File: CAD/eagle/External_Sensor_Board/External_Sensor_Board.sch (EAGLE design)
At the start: 14 parts, among them J1 SFW15R_FFC, J2 J30J-25, U1 MAX31725MTA+, U2 HSCMNNN1.6BAAA3, U3 P82B715

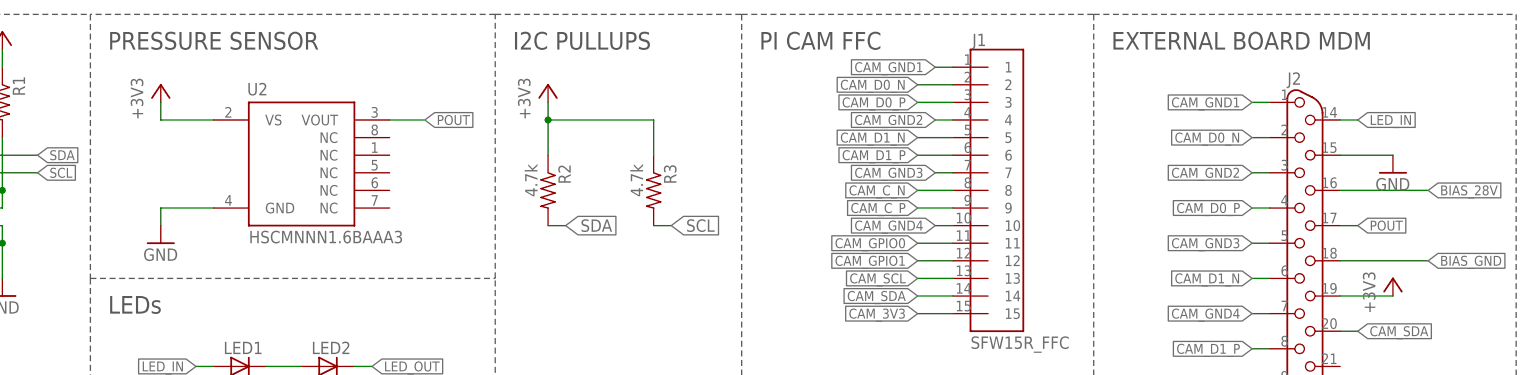
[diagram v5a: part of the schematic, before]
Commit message: Began work on pressure sensor library. Realized I specced an inadequate sensor. Specced a better sensor (in the same family). Changed external sensor board to compensate.
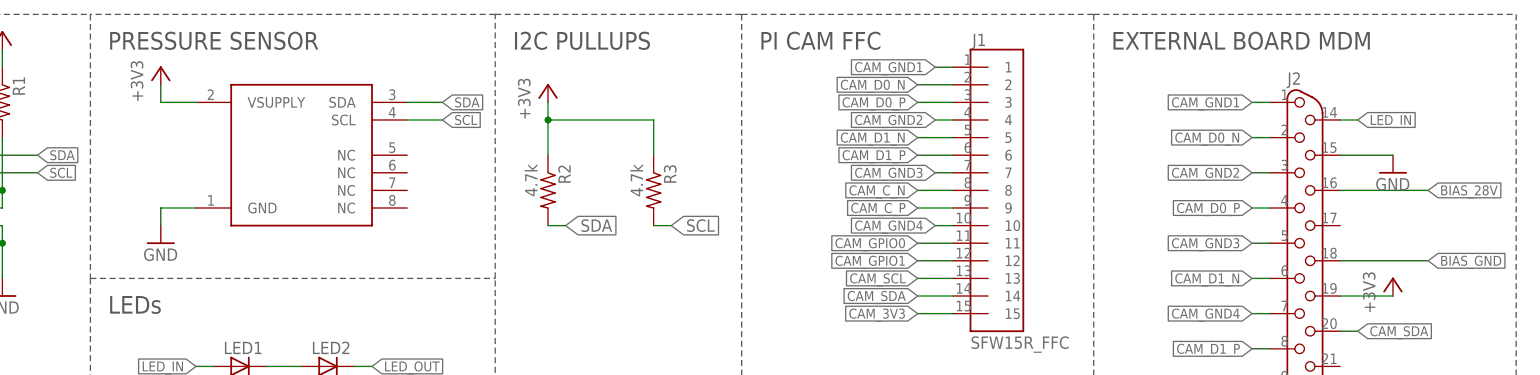
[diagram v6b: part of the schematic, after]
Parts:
- U2: value HSCMNNN1.6BAAA3 -> SSCMNNN015PA2A3; device NR_IC:HSCMNNN1.6BAAA3 -> NR_IC:SSCMNNN015PA2A3
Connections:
- removed net POUT: J2.17, U2.VOUT
- net +3V3: now also U2.VSUPPLY; no longer U2.VS
- net SCL: now also U2.SCL
- net SDA: now also U2.SDA
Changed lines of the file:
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@@
 <part name="R1" library="resistor" deviceset="R-US_" device="R0603" value="4.7k"/>
 <part name="GND2" library="supply1" deviceset="GND" device=""/>
-<part name="U2" library="NR_IC" deviceset="HSCMNNN1.6BAAA3" device=""/>
 <part name="+3V3" library="supply1" deviceset="+3V3" device=""/>
 <part name="GND3" library="supply1" deviceset="GND" device=""/>
@@
 <part name="GND7" library="supply1" deviceset="GND" device=""/>
 <part name="JP1" library="pinhead" deviceset="PINHD-1X2" device=""/>
+<part name="U2" library="NR_IC" deviceset="SSCMNNN015PA2A3" device=""/>
 </parts>
 <sheets>
@@
 <instance part="R1" gate="G$1" x="55.88" y="195.58" rot="R270"/>
 <instance part="GND2" gate="1" x="55.88" y="167.64"/>
-<instance part="U2" gate="G$1" x="99.06" y="187.96"/>
-<instance part="+3V3" gate="G$1" x="78.74" y="198.12"/>
+<instance part="+3V3" gate="G$1" x="78.74" y="200.66"/>
 <instance part="GND3" gate="1" x="78.74" y="175.26"/>
 <instance part="+3V4" gate="G$1" x="134.62" y="198.12"/>
@@
 <instance part="GND7" gate="1" x="256.54" y="185.42"/>
 <instance part="JP1" gate="G$1" x="104.14" y="137.16"/>
+<instance part="U2" gate="G$1" x="99.06" y="187.96"/>
 </instances>
 <busses>
@@
 <pinref part="R1" gate="G$1" pin="1"/>
 <wire x1="55.88" y1="203.2" x2="55.88" y2="200.66" width="0.1524" layer="91"/>
-</segment>
-<segment>
-<pinref part="+3V3" gate="G$1" pin="+3V3"/>
-<pinref part="U2" gate="G$1" pin="VS"/>
-<wire x1="78.74" y1="195.58" x2="78.74" y2="193.04" width="0.1524" layer="91"/>
-<wire x1="78.74" y1="193.04" x2="86.36" y2="193.04" width="0.1524" layer="91"/>
 </segment>
 <segment>
@@
 <pinref part="+3V7" gate="G$1" pin="+3V3"/>
 <wire x1="248.92" y1="167.64" x2="256.54" y2="167.64" width="0.1524" layer="91"/>
+</segment>
+<segment>
+<pinref part="+3V3" gate="G$1" pin="+3V3"/>
+<pinref part="U2" gate="G$1" pin="VSUPPLY"/>
+<wire x1="78.74" y1="198.12" x2="78.74" y2="195.58" width="0.1524" layer="91"/>
+<wire x1="78.74" y1="195.58" x2="83.82" y2="195.58" width="0.1524" layer="91"/>
 </segment>
 </net>
@@
 </segment>
 <segment>
-<pinref part="U2" gate="G$1" pin="GND"/>
-<pinref part="GND3" gate="1" pin="GND"/>
-<wire x1="86.36" y1="180.34" x2="78.74" y2="180.34" width="0.1524" layer="91"/>
-<wire x1="78.74" y1="180.34" x2="78.74" y2="177.8" width="0.1524" layer="91"/>
-</segment>
-<segment>
 <pinref part="U3" gate="G$1" pin="GND"/>
 <pinref part="GND5" gate="1" pin="GND"/>
@@
 <wire x1="248.92" y1="187.96" x2="256.54" y2="187.96" width="0.1524" layer="91"/>
 </segment>
+<segment>
+<pinref part="GND3" gate="1" pin="GND"/>
+<pinref part="U2" gate="G$1" pin="GND"/>
+<wire x1="78.74" y1="177.8" x2="78.74" y2="180.34" width="0.1524" layer="91"/>
+<wire x1="78.74" y1="180.34" x2="83.82" y2="180.34" width="0.1524" layer="91"/>
+</segment>
 </net>
 <net name="SDA" class="0">
@@
 <label x="50.8" y="121.92" size="1.016" layer="95" xref="yes"/>
 </segment>
+<segment>
+<pinref part="U2" gate="G$1" pin="SDA"/>
+<wire x1="114.3" y1="195.58" x2="119.38" y2="195.58" width="0.1524" layer="91"/>
+<label x="119.38" y="195.58" size="1.4224" layer="95" xref="yes"/>
+</segment>
 </net>
 <net name="SCL" class="0">
@@
 <wire x1="22.86" y1="121.92" x2="20.32" y2="121.92" width="0.1524" layer="91"/>
 <label x="20.32" y="121.92" size="1.016" layer="95" rot="R180" xref="yes"/>
+</segment>
+<segment>
+<pinref part="U2" gate="G$1" pin="SCL"/>
+<wire x1="114.3" y1="193.04" x2="119.38" y2="193.04" width="0.1524" layer="91"/>
+<label x="119.38" y="193.04" size="1.4224" layer="95" xref="yes"/>
 </segment>
 </net>
@@
 </segment>
 </net>
-<net name="POUT" class="0">
-<segment>
-<pinref part="U2" gate="G$1" pin="VOUT"/>
-<wire x1="111.76" y1="193.04" x2="116.84" y2="193.04" width="0.1524" layer="91"/>
-<label x="116.84" y="193.04" size="1.4224" layer="95" xref="yes"/>
-</segment>
-<segment>
-<pinref part="J2" gate="G$1" pin="17"/>
-<wire x1="248.92" y1="177.8" x2="251.46" y2="177.8" width="0.1524" layer="91"/>
-<label x="251.46" y="177.8" size="1.4224" layer="95" xref="yes"/>
-</segment>
-</net>

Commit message: Final layouts and gerbers
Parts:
- added U$1: SSL.3IN_SILK, images:SSL.3IN_SILK
- added U$2: STAR, images:STAR
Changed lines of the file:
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@@
 <?xml version="1.0" encoding="utf-8"?>
 <!DOCTYPE eagle SYSTEM "eagle.dtd">
-<eagle version="7.7.0">
+<eagle version="6.5.0">
 <drawing>
 <settings>
@@
 <layer number="2" name="Route2" color="1" fill="3" visible="no" active="no"/>
 <layer number="3" name="Route3" color="4" fill="3" visible="no" active="no"/>
+<layer number="4" name="Route4" color="1" fill="4" visible="no" active="no"/>
+<layer number="5" name="Route5" color="4" fill="4" visible="no" active="no"/>
+<layer number="6" name="Route6" color="1" fill="8" visible="no" active="no"/>
+<layer number="7" name="Route7" color="4" fill="8" visible="no" active="no"/>
+<layer number="8" name="Route8" color="1" fill="2" visible="no" active="no"/>
+<layer number="9" name="Route9" color="4" fill="2" visible="no" active="no"/>
+<layer number="10" name="Route10" color="1" fill="7" visible="no" active="no"/>
+<layer number="11" name="Route11" color="4" fill="7" visible="no" active="no"/>
+<layer number="12" name="Route12" color="1" fill="5" visible="no" active="no"/>
+<layer number="13" name="Route13" color="4" fill="5" visible="no" active="no"/>
 <layer number="14" name="Route14" color="1" fill="6" visible="no" active="no"/>
 <layer number="15" name="Route15" color="4" fill="6" visible="no" active="no"/>
@@
 <part name="JP1" library="pinhead" deviceset="PINHD-1X2" device=""/>
 <part name="U2" library="NR_IC" deviceset="SSCMNNN015PA2A3" device=""/>
+<part name="U$1" library="images" deviceset="SSL" device=".3IN_SILK"/>
+<part name="U$2" library="images" deviceset="STAR" device=""/>
 </parts>
 <sheets>
@@
 <instance part="JP1" gate="G$1" x="104.14" y="137.16"/>
 <instance part="U2" gate="G$1" x="99.06" y="187.96"/>
+<instance part="U$1" gate="G$1" x="264.16" y="48.26"/>
+<instance part="U$2" gate="G$1" x="246.38" y="43.18"/>
 </instances>
 <busses>

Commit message: Beginning rework of expternal sensor board.
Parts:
- removed C2: 1uF, resistor:C-USC0603
- removed C3: 100nF, resistor:C-USC0603
- removed U3: P82B715, CM_IC:P82B715
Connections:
- removed net SCL_BUFF: J2.25, U3.LX
- removed net SDA_BUFF: J2.23, U3.LY
- net +3V3: no longer C2.1, C3.1, U3.VCC
- net GND: no longer C2.2, C3.2, U3.GND
- net SCL: now also J2.25; no longer U3.SX
- net SDA: now also J2.23; no longer U3.SY
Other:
- note removed: "I2C BUFFER"
- moved on the sheet: JP1
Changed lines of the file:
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@@
 <?xml version="1.0" encoding="utf-8"?>
 <!DOCTYPE eagle SYSTEM "eagle.dtd">
-<eagle version="6.5.0">
+<eagle version="7.7.0">
 <drawing>
 <settings>
@@
 <part name="LED1" library="NR_LED" deviceset="LED_1206_NS" device=""/>
 <part name="LED2" library="NR_LED" deviceset="LED_1206_NS" device=""/>
-<part name="U3" library="CM_IC" deviceset="P82B715" device=""/>
-<part name="GND5" library="supply1" deviceset="GND" device=""/>
-<part name="+3V6" library="supply1" deviceset="+3V3" device=""/>
-<part name="C2" library="resistor" deviceset="C-US" device="C0603" value="1uF"/>
-<part name="C3" library="resistor" deviceset="C-US" device="C0603" value="100nF"/>
-<part name="GND6" library="supply1" deviceset="GND" device=""/>
 <part name="J2" library="CM_J30J" deviceset="J30J-25" device=""/>
 <part name="+3V7" library="supply1" deviceset="+3V3" device=""/>
@@
 <wire x1="68.58" y1="208.28" x2="68.58" y2="170.18" width="0.1524" layer="97" style="shortdash"/>
 <wire x1="68.58" y1="170.18" x2="68.58" y2="152.4" width="0.1524" layer="97" style="shortdash"/>
-<wire x1="68.58" y1="152.4" x2="7.62" y2="152.4" width="0.1524" layer="97" style="shortdash"/>
+<wire x1="68.58" y1="152.4" x2="55.88" y2="152.4" width="0.1524" layer="97" style="shortdash"/>
+<wire x1="55.88" y1="152.4" x2="7.62" y2="152.4" width="0.1524" layer="97" style="shortdash"/>
 <wire x1="7.62" y1="152.4" x2="7.62" y2="208.28" width="0.1524" layer="97" style="shortdash"/>
 <text x="71.12" y="203.2" size="2.54" layer="97">PRESSURE SENSOR</text>
-<wire x1="68.58" y1="152.4" x2="71.12" y2="152.4" width="0.1524" layer="97" style="shortdash"/>
-<wire x1="71.12" y1="152.4" x2="119.38" y2="152.4" width="0.1524" layer="97" style="shortdash"/>
-<wire x1="119.38" y1="152.4" x2="127" y2="152.4" width="0.1524" layer="97" style="shortdash"/>
+<wire x1="68.58" y1="152.4" x2="127" y2="152.4" width="0.1524" layer="97" style="shortdash"/>
 <wire x1="127" y1="152.4" x2="127" y2="170.18" width="0.1524" layer="97" style="shortdash"/>
 <wire x1="127" y1="170.18" x2="127" y2="208.28" width="0.1524" layer="97" style="shortdash"/>
@@
 <text x="71.12" y="165.1" size="2.54" layer="97">LEDs</text>
 <wire x1="68.58" y1="170.18" x2="127" y2="170.18" width="0.1524" layer="97" style="shortdash"/>
-<text x="10.16" y="147.32" size="2.54" layer="97">I2C BUFFER</text>
-<wire x1="7.62" y1="152.4" x2="7.62" y2="109.22" width="0.1524" layer="97" style="shortdash"/>
-<wire x1="7.62" y1="109.22" x2="71.12" y2="109.22" width="0.1524" layer="97" style="shortdash"/>
-<wire x1="71.12" y1="109.22" x2="71.12" y2="129.54" width="0.1524" layer="97" style="shortdash"/>
-<wire x1="71.12" y1="129.54" x2="71.12" y2="152.4" width="0.1524" layer="97" style="shortdash"/>
 <wire x1="274.32" y1="121.92" x2="213.36" y2="121.92" width="0.1524" layer="97" style="shortdash"/>
 <wire x1="213.36" y1="121.92" x2="213.36" y2="152.4" width="0.1524" layer="97" style="shortdash"/>
-<text x="73.66" y="147.32" size="2.54" layer="97">28V BIAS FRAMEWORK</text>
-<wire x1="71.12" y1="129.54" x2="119.38" y2="129.54" width="0.1524" layer="97" style="shortdash"/>
-<wire x1="119.38" y1="129.54" x2="119.38" y2="152.4" width="0.1524" layer="97" style="shortdash"/>
+<text x="10.16" y="147.32" size="2.54" layer="97">28V BIAS FRAMEWORK</text>
+<wire x1="7.62" y1="152.4" x2="7.62" y2="129.54" width="0.1524" layer="97" style="shortdash"/>
+<wire x1="7.62" y1="129.54" x2="55.88" y2="129.54" width="0.1524" layer="97" style="shortdash"/>
+<wire x1="55.88" y1="129.54" x2="55.88" y2="152.4" width="0.1524" layer="97" style="shortdash"/>
 </plain>
 <instances>
@@
 <instance part="LED1" gate="G$1" x="91.44" y="157.48" rot="R90"/>
 <instance part="LED2" gate="G$1" x="104.14" y="157.48" rot="R90"/>
-<instance part="U3" gate="G$1" x="35.56" y="121.92"/>
-<instance part="GND5" gate="1" x="20.32" y="114.3"/>
-<instance part="+3V6" gate="G$1" x="50.8" y="147.32"/>
-<instance part="C2" gate="G$1" x="53.34" y="139.7" rot="R90"/>
-<instance part="C3" gate="G$1" x="53.34" y="129.54" rot="R90"/>
-<instance part="GND6" gate="1" x="66.04" y="124.46"/>
 <instance part="J2" gate="G$1" x="243.84" y="165.1"/>
 <instance part="+3V7" gate="G$1" x="256.54" y="170.18"/>
 <instance part="GND7" gate="1" x="256.54" y="185.42"/>
-<instance part="JP1" gate="G$1" x="104.14" y="137.16"/>
+<instance part="JP1" gate="G$1" x="40.64" y="137.16"/>
 <instance part="U2" gate="G$1" x="99.06" y="187.96"/>
 <instance part="U$1" gate="G$1" x="264.16" y="48.26"/>
@@
 <wire x1="149.86" y1="193.04" x2="149.86" y2="187.96" width="0.1524" layer="91"/>
 <junction x="134.62" y="193.04"/>
-</segment>
-<segment>
-<pinref part="+3V6" gate="G$1" pin="+3V3"/>
-<pinref part="C2" gate="G$1" pin="1"/>
-<wire x1="50.8" y1="144.78" x2="50.8" y2="139.7" width="0.1524" layer="91"/>
-<pinref part="C3" gate="G$1" pin="1"/>
-<wire x1="50.8" y1="139.7" x2="50.8" y2="129.54" width="0.1524" layer="91"/>
-<junction x="50.8" y="139.7"/>
-<pinref part="U3" gate="G$1" pin="VCC"/>
-<wire x1="50.8" y1="129.54" x2="50.8" y2="127" width="0.1524" layer="91"/>
-<wire x1="50.8" y1="127" x2="48.26" y2="127" width="0.1524" layer="91"/>
-<junction x="50.8" y="129.54"/>
 </segment>
 <segment>
@@
 </segment>
 <segment>
-<pinref part="U3" gate="G$1" pin="GND"/>
-<pinref part="GND5" gate="1" pin="GND"/>
-<wire x1="22.86" y1="119.38" x2="20.32" y2="119.38" width="0.1524" layer="91"/>
-<wire x1="20.32" y1="119.38" x2="20.32" y2="116.84" width="0.1524" layer="91"/>
-</segment>
-<segment>
-<pinref part="C3" gate="G$1" pin="2"/>
-<pinref part="GND6" gate="1" pin="GND"/>
-<wire x1="58.42" y1="129.54" x2="66.04" y2="129.54" width="0.1524" layer="91"/>
-<wire x1="66.04" y1="129.54" x2="66.04" y2="127" width="0.1524" layer="91"/>
-<pinref part="C2" gate="G$1" pin="2"/>
-<wire x1="66.04" y1="129.54" x2="66.04" y2="139.7" width="0.1524" layer="91"/>
-<wire x1="66.04" y1="139.7" x2="58.42" y2="139.7" width="0.1524" layer="91"/>
-<junction x="66.04" y="129.54"/>
-</segment>
-<segment>
 <pinref part="J2" gate="G$1" pin="15"/>
 <pinref part="GND7" gate="1" pin="GND"/>
@@
 </segment>
 <segment>
-<pinref part="U3" gate="G$1" pin="SY"/>
-<wire x1="48.26" y1="121.92" x2="50.8" y2="121.92" width="0.1524" layer="91"/>
-<label x="50.8" y="121.92" size="1.016" layer="95" xref="yes"/>
-</segment>
-<segment>
 <pinref part="U2" gate="G$1" pin="SDA"/>
 <wire x1="114.3" y1="195.58" x2="119.38" y2="195.58" width="0.1524" layer="91"/>
 <label x="119.38" y="195.58" size="1.4224" layer="95" xref="yes"/>
 </segment>
+<segment>
+<pinref part="J2" gate="G$1" pin="23"/>
+<wire x1="248.92" y1="147.32" x2="251.46" y2="147.32" width="0.1524" layer="91"/>
+<label x="251.46" y="147.32" size="1.4224" layer="95" xref="yes"/>
+</segment>
 </net>
 <net name="SCL" class="0">
@@
 </segment>
 <segment>
-<pinref part="U3" gate="G$1" pin="SX"/>
-<wire x1="22.86" y1="121.92" x2="20.32" y2="121.92" width="0.1524" layer="91"/>
-<label x="20.32" y="121.92" size="1.016" layer="95" rot="R180" xref="yes"/>
-</segment>
-<segment>
 <pinref part="U2" gate="G$1" pin="SCL"/>
 <wire x1="114.3" y1="193.04" x2="119.38" y2="193.04" width="0.1524" layer="91"/>
 <label x="119.38" y="193.04" size="1.4224" layer="95" xref="yes"/>
+</segment>
+<segment>
+<pinref part="J2" gate="G$1" pin="25"/>
+<wire x1="248.92" y1="137.16" x2="251.46" y2="137.16" width="0.1524" layer="91"/>
+<label x="251.46" y="137.16" size="1.4224" layer="95" xref="yes"/>
 </segment>
 </net>
@@
 </segment>
 </net>
-<net name="SDA_BUFF" class="0">
-<segment>
-<pinref part="U3" gate="G$1" pin="LY"/>
-<wire x1="48.26" y1="124.46" x2="50.8" y2="124.46" width="0.1524" layer="91"/>
-<label x="50.8" y="124.46" size="1.016" layer="95" xref="yes"/>
-</segment>
-<segment>
-<pinref part="J2" gate="G$1" pin="23"/>
-<wire x1="248.92" y1="147.32" x2="251.46" y2="147.32" width="0.1524" layer="91"/>
-<label x="251.46" y="147.32" size="1.4224" layer="95" xref="yes"/>
-</segment>
-</net>
-<net name="SCL_BUFF" class="0">
-<segment>
-<pinref part="U3" gate="G$1" pin="LX"/>
-<wire x1="22.86" y1="124.46" x2="20.32" y2="124.46" width="0.1524" layer="91"/>
-<label x="20.32" y="124.46" size="1.016" layer="95" rot="R180" xref="yes"/>
-</segment>
-<segment>
-<pinref part="J2" gate="G$1" pin="25"/>
-<wire x1="248.92" y1="137.16" x2="251.46" y2="137.16" width="0.1524" layer="91"/>
-<label x="251.46" y="137.16" size="1.4224" layer="95" xref="yes"/>
-</segment>
-</net>
 <net name="BIAS_28V" class="0">
 <segment>
 <pinref part="JP1" gate="G$1" pin="1"/>
-<wire x1="101.6" y1="139.7" x2="93.98" y2="139.7" width="0.1524" layer="91"/>
-<label x="93.98" y="139.7" size="1.4224" layer="95" rot="R180" xref="yes"/>
+<wire x1="38.1" y1="139.7" x2="30.48" y2="139.7" width="0.1524" layer="91"/>
+<label x="30.48" y="139.7" size="1.4224" layer="95" rot="R180" xref="yes"/>
 </segment>
 <segment>
@@
 <segment>
 <pinref part="JP1" gate="G$1" pin="2"/>
-<wire x1="101.6" y1="137.16" x2="93.98" y2="137.16" width="0.1524" layer="91"/>
-<label x="93.98" y="137.16" size="1.4224" layer="95" rot="R180" xref="yes"/>
-</segment>
-<segment>
+<wire x1="38.1" y1="137.16" x2="30.48" y2="137.16" width="0.1524" layer="91"/>
+<label x="30.48" y="137.16" size="1.4224" layer="95" rot="R180" xref="yes"/>
+</segment>
+<segment>
